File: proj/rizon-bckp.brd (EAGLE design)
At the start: 99.1 x 80 mm, 32 parts, among them J1 PWRJACK5521, P1 ADDR, P2 DATA, P3 CTL, P4 PWR, P5 10k, U1 Z8400, U2 AS6C62256PDIP, U3 AS6C62256PDIP, U4 AT28C64BPLCC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

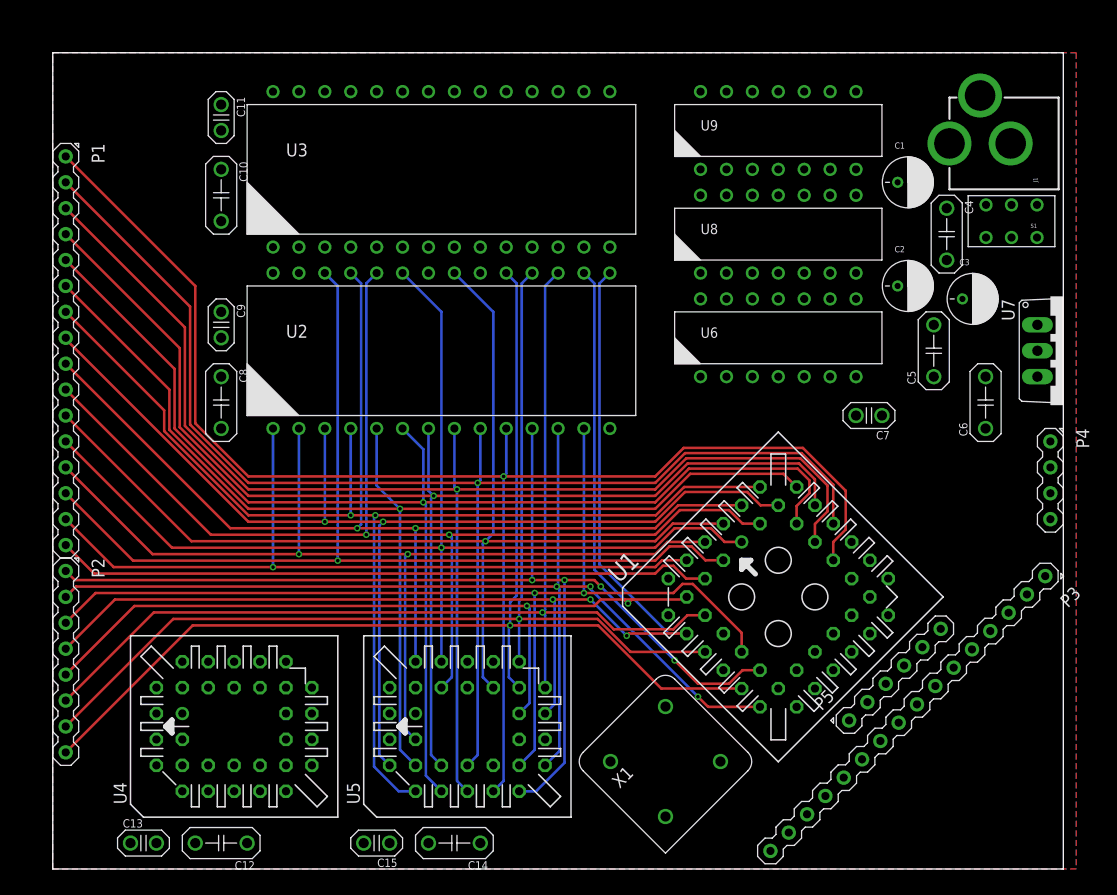
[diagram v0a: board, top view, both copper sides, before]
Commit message: Redesigning Rizon board
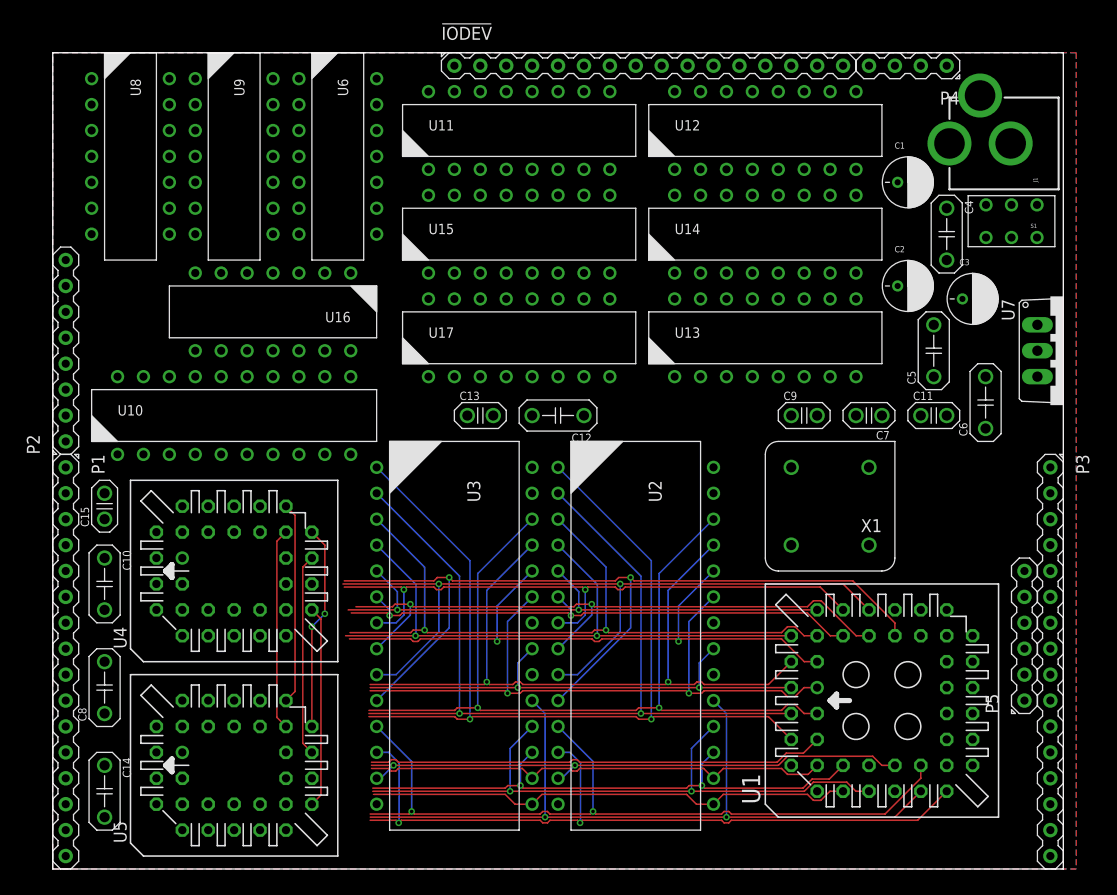
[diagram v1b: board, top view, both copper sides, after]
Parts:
- added !IODEV: ADDR, dooba:PIN_16
- added U10: 74273PDIP, dooba:PDIP20
- added U11, U12, U13, U14, U15, U17: 74138PDIP, dooba:PDIP16
- added U16: 7432PDIP, dooba:PDIP14
- moved C11 75.7 mm to (86.4, 44.5), turned to 0 degrees
- moved U8 64.0 mm to (7.62, 69.8), turned to 270 degrees
- moved C9 57.8 mm to (73.7, 44.5), turned to 0 degrees
- moved U9 53.4 mm to (17.8, 69.8), turned to 270 degrees
- moved C12 53.4 mm to (49.5, 44.5)
- moved C13 53.4 mm to (41.9, 44.5)
- moved U6 46.7 mm to (27.9, 69.8), turned to 270 degrees
- moved U3 45.7 mm to (39.4, 22.9), turned to 270 degrees
- moved P4 43.0 mm to (83.8, 78.7), turned to 180 degrees
- moved C15 42.4 mm to (5.08, 35.6), turned to 90 degrees
- moved C10 39.8 mm to (5.08, 27.9)
- moved C14 34.7 mm to (5.08, 7.62), turned to 270 degrees
- moved U2 33.8 mm to (57.1, 22.9), turned to 270 degrees
- moved P1 30.5 mm to (1.27, 20.3)
- moved P2 30.5 mm to (1.27, 50.8), turned to 90 degrees
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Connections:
- net ROM_EN renamed SCR0_ROM_EN
- removed net !ROM_EN: P3.14, U6.P$2, U9.P$10, U9.P$9
- new net !IODEV0: U11.P$15, U16.P$1
- new net !IODEV1: !IODEV.2, U11.P$14
- new net !IODEV10: !IODEV.11, U12.P$13
- new net !IODEV11: !IODEV.12, U12.P$12
- new net !IODEV12: !IODEV.13, U12.P$11
- new net !IODEV13: !IODEV.14, U12.P$10
- new net !IODEV14: !IODEV.15, U12.P$9
- new net !IODEV15: !IODEV.16, U12.P$7
- new net !IODEV2: !IODEV.3, U11.P$13
- new net !IODEV3: !IODEV.4, U11.P$12
- new net !IODEV4: !IODEV.5, U11.P$11
- new net !IODEV5: !IODEV.6, U11.P$10
- new net !IODEV6: !IODEV.7, U11.P$9
- new net !IODEV7: !IODEV.8, U11.P$7
- new net !IODEV8: !IODEV.9, U12.P$15
- new net !IODEV9: !IODEV.10, U12.P$14
- new net !IO_SELECT_BANK0: U11.P$5, U13.P$15
- new net !IO_SELECT_BANK1: U12.P$4, U13.P$14
- new net !SCR0_CP: U16.P$3, U9.P$12, U9.P$13
- new net !SCR0_ROM_EN: U10.P$2, U6.P$2, U9.P$10, U9.P$9
- new net N$1: U13.P$5, U14.P$15
- new net N$2: U14.P$5, U15.P$15
- new net N$3: U15.P$5, U17.P$15
- new net SCR0_CP: U10.P$11, U9.P$11
- net !IORQ: now also U11.P$4, U12.P$5, U13.P$4, U14.P$4, U15.P$4, U17.P$4
- net !M1: now also U11.P$6, U12.P$6, U13.P$6, U14.P$6, U15.P$6, U17.P$6
- net !RESET: now also U10.P$1
- net !WR: now also U16.P$2
- net ADDR0: now also U11.P$1, U12.P$1
- net ADDR1: now also U11.P$2, U12.P$2
- net ADDR10: now also U15.P$2
- net ADDR11: now also U15.P$3
- net ADDR12: now also U17.P$1
- net ADDR13: now also U17.P$2
- net ADDR14: now also U17.P$3
- net ADDR15: now also U17.P$5
- net ADDR2: now also U11.P$3, U12.P$3
- net ADDR3: now also U13.P$1
- net ADDR4: now also U13.P$2
- net ADDR5: now also U13.P$3
- net ADDR6: now also U14.P$1
- net ADDR7: now also U14.P$2
- net ADDR8: now also U14.P$3
- net ADDR9: now also U15.P$1
- net DATA0: now also U10.P$3
- net DATA1: now also U10.P$4
- net DATA2: now also U10.P$7
- net DATA3: now also U10.P$8
- net DATA4: now also U10.P$13
- net DATA5: now also U10.P$14
- net DATA6: now also U10.P$17
- net DATA7: now also U10.P$18
- net GND: now also !IODEV.1, P3.14, U10.P$10, U11.P$8, U12.P$8, U13.P$8, U14.P$8, U15.P$8, U16.P$7, U17.P$8
- net VCC: now also U10.P$20, U11.P$16, U12.P$16, U13.P$16, U14.P$16, U15.P$16, U16.P$14, U17.P$16
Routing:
- net ADDR4: track 129.9 -> 54.4 mm, vias 1 -> 2
- net ADDR2: track 136.2 -> 63.8 mm, vias 1 -> 2
- net ADDR3: track 126.9 -> 61.6 mm, vias 1 -> 2
- net DATA4: track 110.6 -> 46.3 mm, vias 2 -> 0
- net ADDR5: track 119.6 -> 55.3 mm, vias 1 -> 2
- net ADDR10: track 113.3 -> 50.1 mm, vias 1 -> 2
- net ADDR1: track 134.1 -> 77.7 mm, vias 1 -> 2
- net ADDR0: track 143.6 -> 87.5 mm, vias 1 -> 2
- net ADDR9: track 117.1 -> 64.4 mm
- net ADDR6: track 116.9 -> 64.7 mm
- net DATA2: track 105.3 -> 56.4 mm
- net DATA3: track 116.4 -> 68.0 mm, vias 3 -> 0
- net ADDR11: track 111.6 -> 65.9 mm, vias 1 -> 2
- net ADDR7: track 112.7 -> 72.5 mm
- net ADDR8: track 112.5 -> 73.6 mm
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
